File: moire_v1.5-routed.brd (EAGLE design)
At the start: 39.4 x 106.7 mm, 135 parts, among them IC1 R-78E3.3-0.5, IC100 LM324PW, IC101 TLC59281DBQ, IC102 4051PW, IC103 LM4040B25, IC104 LD2981ABU33, J1 PJ301_THONKICONN6, J10 PJ301_THONKICONN6, J11 PJ301_THONKICONN6, J12 PJ301_THONKICONN6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

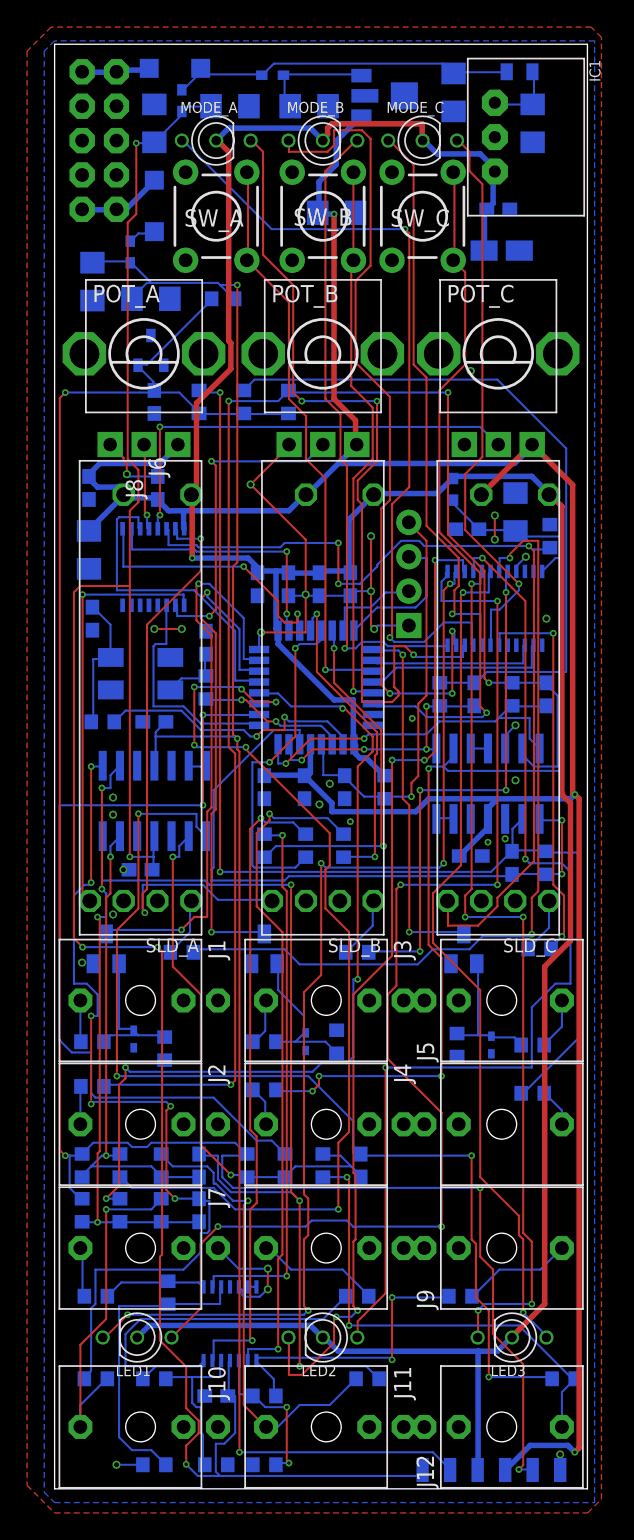
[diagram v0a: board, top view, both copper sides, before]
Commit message: resolve drc errors
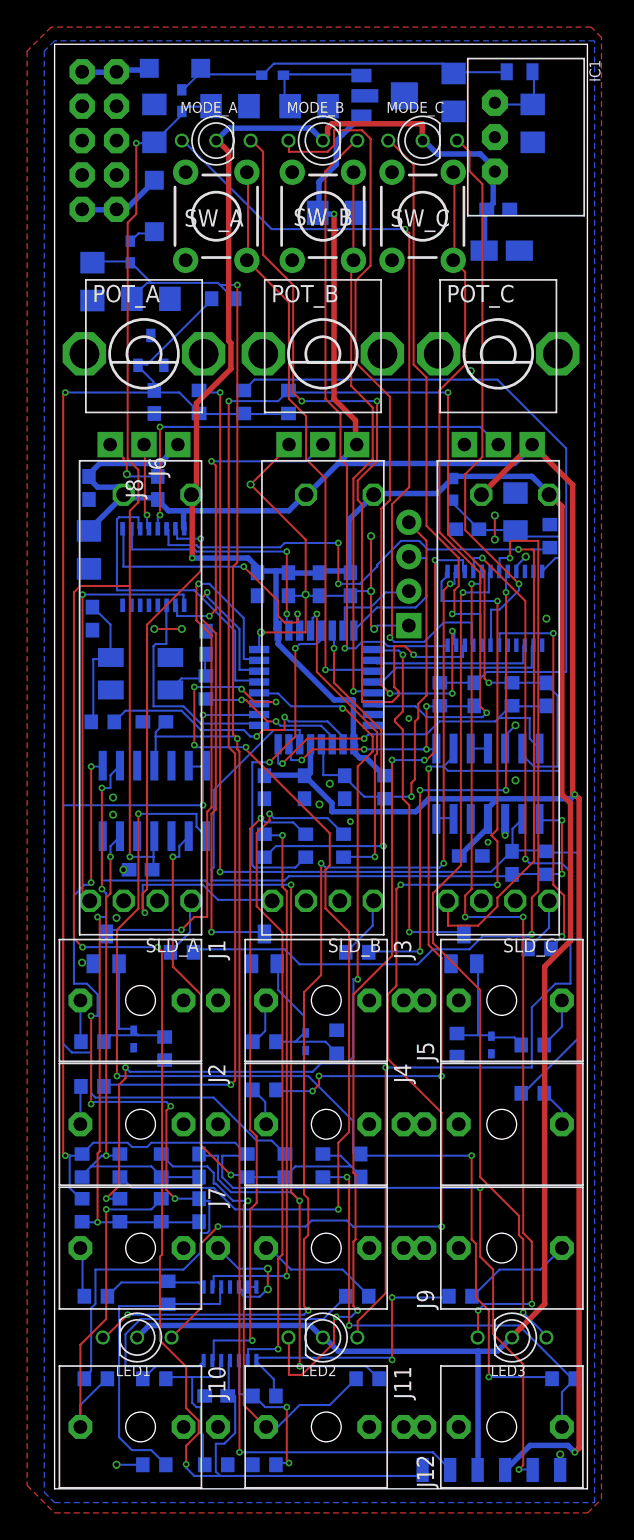
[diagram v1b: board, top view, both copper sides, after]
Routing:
- net N$45: track 60.3 -> 60.8 mm
